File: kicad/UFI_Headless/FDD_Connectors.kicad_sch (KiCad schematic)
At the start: 11 parts, among them J6 FDD_34PIN, J7 AMIGA_FDD

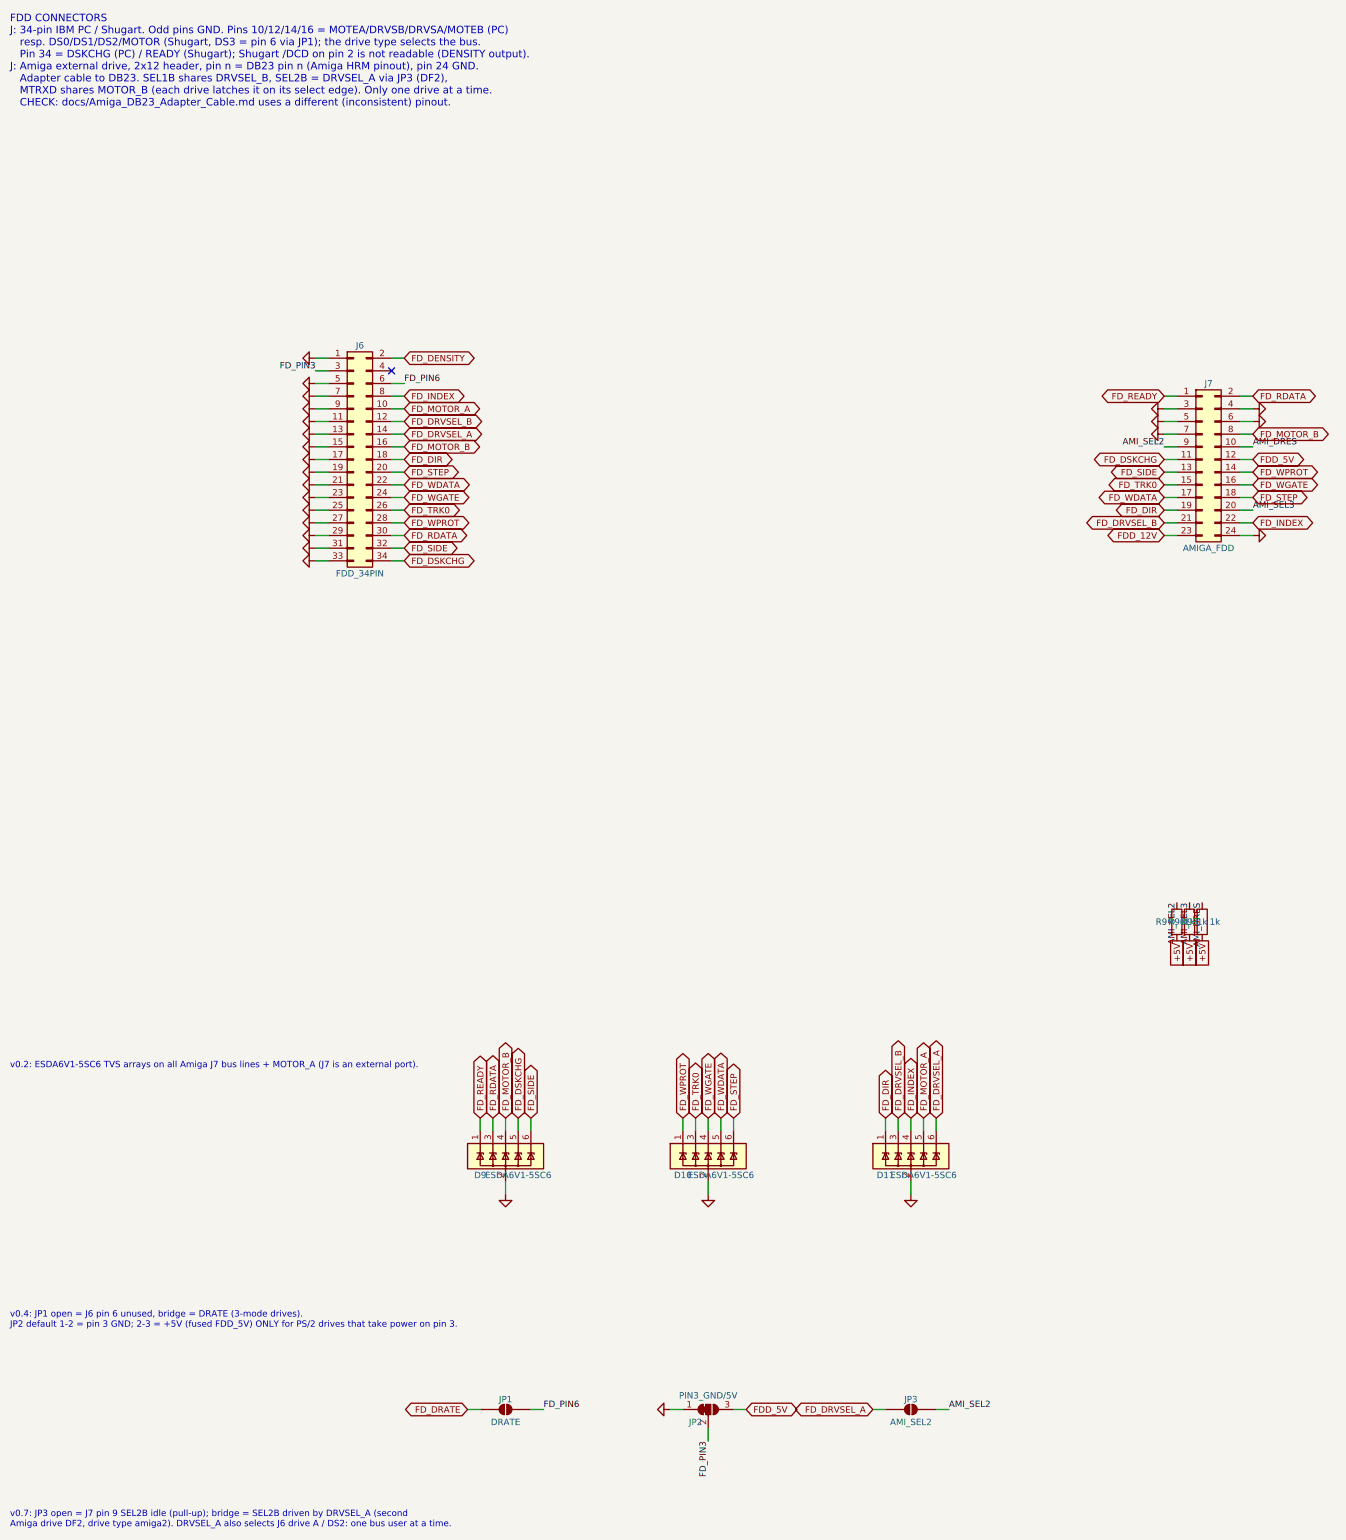
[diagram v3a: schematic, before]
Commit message: KiCad v0.7 rework, stage A11a (owner's device-comparison list M1, M4, M6): write lock gates both write requests, terminations on FDD_5V, JP2 gone - Flux_Interface: U14 becomes a 74LVC1G32 (Diodes 74LVC1G32SE-7 C460530, SOT-353; was the 74LVC1G332 of A9b) forming the global net LOCK = WLOCK_HW or WLOCK_FW; new U30 74LVC2G32 (Nexperia 74LVC2G32DP,125 C548635, TSSOP-8; single-unit project symbol UFI_Headless:74LVC2G32 because the KiCad multi-unit symbol does not work with the MCP placement, pinout 1 1A 2 1B 3 2Y 4 GND 5 2A 6 2B 7 1Y 8 VCC from the datasheet family) gates FDD_WGATE -> FDD_WGATE_G (U7 pin 3, TP8) and APL_WRREQ -> APL_WRREQ_G (new global net to U16 2A2 on Apple_Port, the MCU-side pull-up RN10 stays on APL_WRREQ), C84 100 nF; both requests are active low, LOCK high forces them inactive, so the Apple write request no longer bypasses the lock (netlist: LOCK = U14.4 U30.2 U30.6, APL_WRREQ_G = U16.13 U30.3, FDD_WGATE_G = U7.3 U30.7 TP8.1). M4: R75-R91 (Flux_Interface) and R97-R99 (FDD_Connectors, same reason) pull up to FDD_5V instead of +5V, R92-R96 on the IEC bus stay at +5V. M6: JP2 with its GND symbol and labels removed, J6 pin 3 is GND. Note on the sheet. ERC over the whole project 0 errors / 0 warnings (build/erc.rpt). No firmware change (WLOCK_FW/WLOCK_HW semantics unchanged). PLAN.md A11a done, kicad README A11a row. PCB follows in B3.
Claude-Session: https://claude.ai/code/session_014MdzrcyXuayppPHbfEjUrw
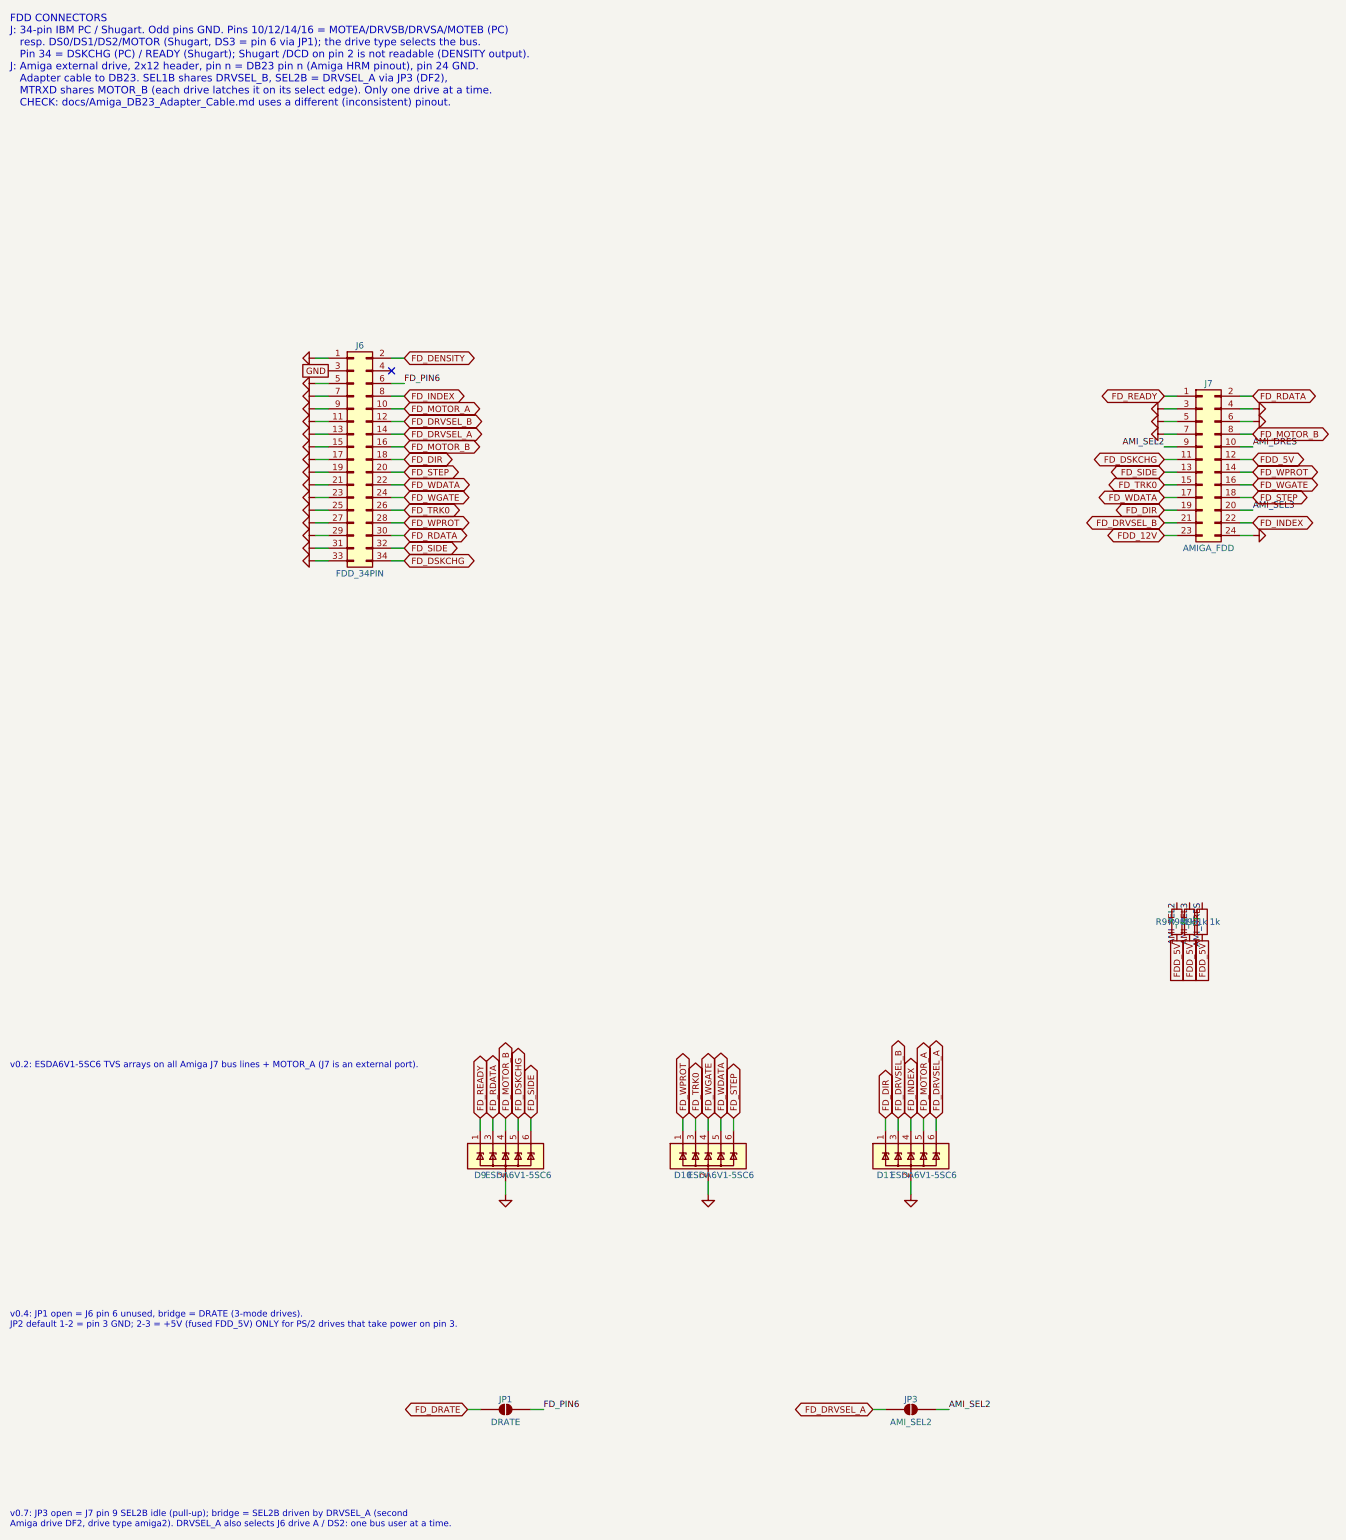
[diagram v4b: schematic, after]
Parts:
- removed JP2: PIN3_GND/5V, Jumper:SolderJumper-3_P1.3mm_Bridged12_RoundedPad1.0x1.5mm, symbol Jumper:SolderJumper_3_Bridged12
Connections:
- net +5V is gone; now on net FDD_5V: R97.2, R98.2, R99.2
- net FD_PIN3 is gone; now on net GND: J6.3 (Pin_3)
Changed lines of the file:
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@@
 		)
 	)
-	(wire
-		(pts
-			(xy 83.82 91.44) (xy 81.28 91.44)
-		)
-		(stroke
-			(width 0)
-			(type default)
-		)
-	)
-	(label "FD_PIN3"
-		(at 81.28 91.44 180)
-		(fields_autoplaced yes)
-		(effects
-			(font
-				(size 1.27 1.27)
-			)
-			(justify right bottom)
-		)
-	)
 	(no_connect
 		(at 96.52 91.44)
@@
 		)
 	)
-	(wire
-		(pts
-			(xy 154.94 299.72) (xy 152.4 299.72)
-		)
-		(stroke
-			(width 0)
-			(type default)
-		)
-	)
-	(wire
-		(pts
-			(xy 160.02 303.53) (xy 160.02 306.07)
-		)
-		(stroke
-			(width 0)
-			(type default)
-		)
-	)
-	(label "FD_PIN3"
-		(at 160.02 306.07 270)
-		(fields_autoplaced yes)
-		(effects
-			(font
-				(size 1.27 1.27)
-			)
-			(justify right bottom)
-		)
-	)
-	(wire
-		(pts
-			(xy 165.1 299.72) (xy 167.64 299.72)
-		)
-		(stroke
-			(width 0)
-			(type default)
-		)
-	)
-	(global_label "FDD_5V"
-		(shape bidirectional)
-		(at 167.64 299.72 0)
-		(fields_autoplaced yes)
-		(effects
-			(font
-				(size 1.27 1.27)
-			)
-			(justify left)
-		)
-		(property "Intersheetrefs" "${INTERSHEET_REFS}"
-			(at 167.64 299.72 0)
-			(effects
-				(font
-					(size 1.27 1.27)
-				)
-				(hide yes)
-			)
-		)
-	)
 	(text "v0.7: JP3 open = J7 pin 9 SEL2B idle (pull-up); bridge = SEL2B driven by DRVSEL_A (second\nAmiga drive DF2, drive type amiga2). DRVSEL_A also selects J6 drive A / DS2: one bus user at a time."
 		(exclude_from_sim no)
@@
 	)
 	(symbol
-		(lib_id "power:GND")
-		(at 152.4 299.72 270)
-		(unit 1)
-		(exclude_from_sim no)
-		(in_bom no)
-		(on_board yes)
-		(dnp no)
-		(property "Reference" "#PWR259"
-			(at 152.4 299.72 0)
-			(effects
-				(font
-					(size 1.27 1.27)
-				)
-				(hide yes)
-			)
-		)
-		(property "Value" "GND"
-			(at 152.4 299.72 0)
-			(effects
-				(font
-					(size 1.27 1.27)
-				)
-				(hide yes)
-			)
-		)
-		(property "Footprint" ""
-			(at 152.4 299.72 0)
-			(effects
-				(font
-					(size 1.27 1.27)
-				)
-				(hide yes)
-			)
-		)
-		(property "Datasheet" ""
-			(at 152.4 299.72 0)
-			(effects
-				(font
-					(size 1.27 1.27)
-				)
-				(hide yes)
-			)
-		)
-		(pin "1"
-		)
-		(instances
-			(project "UFI_Headless"
-				(path "/dc1b800d-cedf-5627-97f0-e6992ff33669/7efa7110-e20d-5bc0-a817-7dc9a25f889d"
-					(reference "#PWR259")
-					(unit 1)
-				)
-			)
-		)
-	)
-	(symbol
-		(lib_id "Jumper:SolderJumper_3_Bridged12")
-		(at 160.02 299.72 0)
-		(unit 1)
-		(exclude_from_sim no)
-		(in_bom no)
-		(on_board yes)
-		(dnp no)
-		(property "Reference" "JP2"
-			(at 157.48 302.26 0)
-			(effects
-				(font
-					(size 1.27 1.27)
-				)
-			)
-		)
-		(property "Value" "PIN3_GND/5V"
-			(at 160.02 296.926 0)
-			(effects
-				(font
-					(size 1.27 1.27)
-				)
-			)
-		)
-		(property "Footprint" "Jumper:SolderJumper-3_P1.3mm_Bridged12_RoundedPad1.0x1.5mm"
-			(at 160.02 299.72 0)
-			(effects
-				(font
-					(size 1.27 1.27)
-				)
-				(hide yes)
-			)
-		)
-		(property "Datasheet" ""
-			(at 160.02 314.96 0)
-			(effects
-				(font
-					(size 1.27 1.27)
-				)
-				(hide yes)
-			)
-		)
-		(pin "1"
-		)
-		(pin "2"
-		)
-		(pin "3"
-		)
-		(instances
-			(project "UFI_Headless"
-				(path "/dc1b800d-cedf-5627-97f0-e6992ff33669/7efa7110-e20d-5bc0-a817-7dc9a25f889d"
-					(reference "JP2")
-					(unit 1)
-				)
-			)
-		)
-	)
-	(symbol
 		(lib_id "Jumper:SolderJumper_2_Open")
 		(at 200.66 299.72 0)
@@
 		)
 	)
-	(global_label "+5V"
+	(global_label "FDD_5V"
 		(at 254.0 205.74 270)
 		(effects
@@
 		)
 	)
-	(global_label "+5V"
+	(global_label "FDD_5V"
 		(at 256.54 205.74 270)
 		(effects
@@
 		)
 	)
-	(global_label "+5V"
+	(global_label "FDD_5V"
 		(at 259.08 205.74 270)
 		(effects
 			(font
+				(size 1.27 1.27)
+			)
+			(justify right)
+		)
+	)
+	(global_label "GND"
+		(at 83.82000000000001 91.44 180)
+		(effects
+			(font

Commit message: KiCad v0.7 rework, stage A11d part 1 (owner's device-comparison list M5, S1-S4, S6; pins per docs/Timer_Zuteilung.md): sync sensor, J6 pin 2/4/33, rail voltage sense - Apple_Port: J19 pin 3 leaves the INDEX bus and becomes SYNC_5V with R165 10k to +3V3 and D30 PESD3V3L1BA, the new third Schmitt inverter U26 74LVC14AD (C133541, single-unit project symbol UFI_Headless:74LVC14_1U) turns it into SYNC -> PC6 (TIM8_CH1, AF3), also reads J6 pin 2 (FD_DENSITY) and pin 4 (FD_PIN4) back as FDD_PIN2_IN -> PD14 / FDD_PIN4_IN -> PD15 and reserves input 9 for the Mac !CSTOUT line of K1 (no-connect until A11d part 2), unused inputs on GND, C86 100 nF. FDD_Connectors: J6 pin 4 gets its own open-drain output Q12 BSS138DW (C154900, channel 1, gate FDD_PIN4 = PF14 with R158 100k, termination R159 1k to FDD_5V); J6 pin 33 moves from a fixed GND to the solder jumper JP7 (bridged to GND by default) whose third pad carries FLIPPY = PB5 through R156 2.2k with R157 2.2k to GND (2.2k instead of the planned 2.4k because 2.2k C4190 is already in the BOM). Power: R160/R161 10k/10k (FDD_5V / 2 -> V_FDD5 = PC4, ADC1 INP4) and R162/R163 33k/10k (FDD_12V / 4.3 -> V_FDD12 = PC5, ADC1 INP8). MCU_Core: no-connects on PC6, PD14, PD15, PF14, PB5, PC4, PC5, PB1 replaced by the global labels; PB0 (MAC_SEL) and PA8 (MAC_PWM) stay no-connect until the Mac header comes in part 2, PB1 = MAC_CSTOUT is already wired to U26. ERC over the whole project 0 errors / 0 warnings (build/erc.rpt). Firmware in the same commit: board.h/board_headless.c define PIN_SYNC, PIN_FDD_PIN2_IN, PIN_FDD_PIN4_IN, PIN_FDD_PIN4, PIN_FDD_PIN33, PIN_MAC_SEL, PIN_MAC_PWM, PIN_MAC_CSTOUT and ADC_CH_V_FDD5/V_FDD12 and initialise them as inputs or released (low) outputs; the TIM8 capture of SYNC, the rail-voltage limits (4.5 V / 10.8 V) and the protocol access follow in stage A10 (protocol doc: one hunk in the INDEX_SIM bullet - the sync sensor no longer drives the INDEX bus on v1.0, apple_sync has no effect there until A10). ARM build 0 wa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
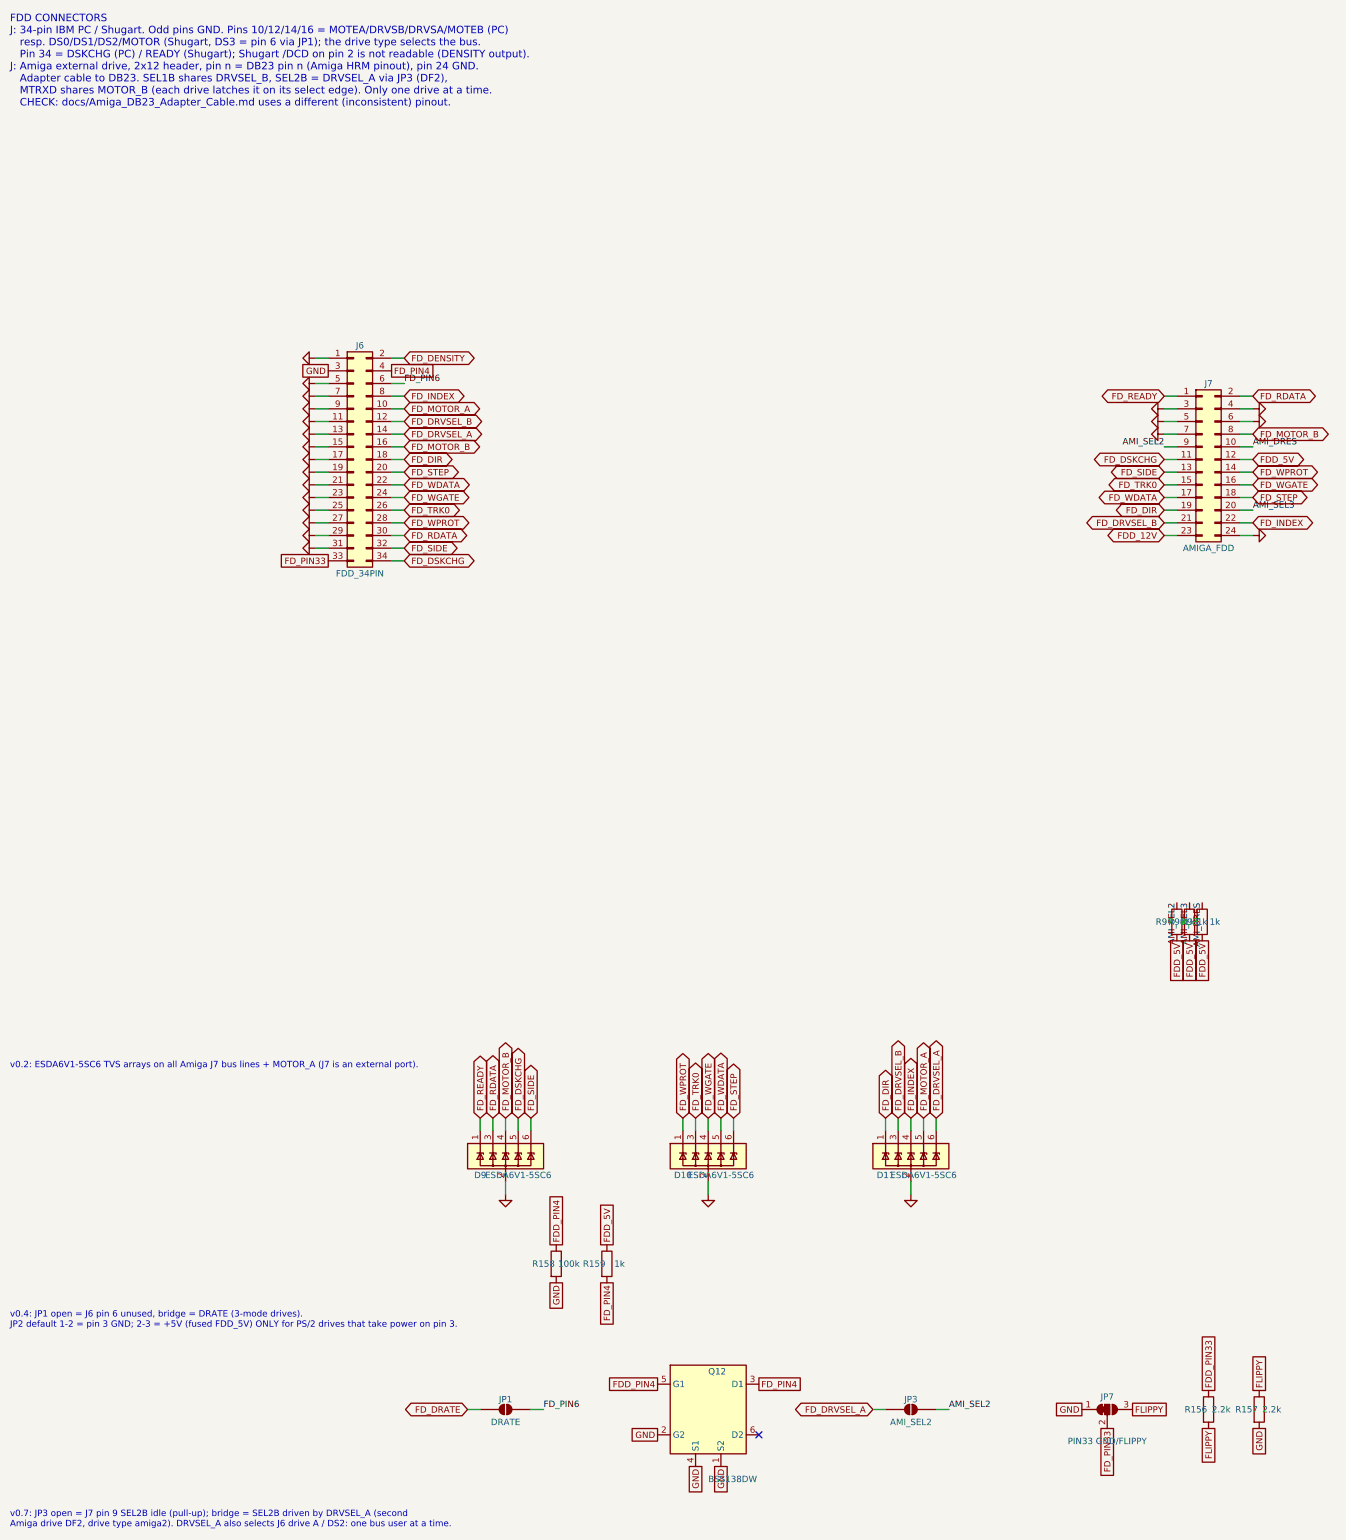
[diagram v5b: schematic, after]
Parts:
- added JP7: PIN33 GND/FLIPPY, Jumper:SolderJumper-3_P1.3mm_Bridged12_RoundedPad1.0x1.5mm, symbol Jumper:SolderJumper_3_Bridged12
- added Q12: BSS138DW, Package_TO_SOT_SMD:SOT-363_SC-70-6, symbol UFI_Headless:BSS138DW
- added R156, R157: 2.2k, Resistor_SMD:R_0603_1608Metric, symbol Device:R
- added R158: 100k, Resistor_SMD:R_0603_1608Metric, symbol Device:R
- added R159: 1k, Resistor_SMD:R_0603_1608Metric, symbol Device:R
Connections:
- net FDD_5V: now also R159.1
- net GND: now also JP7.1 (A), Q12.1 (S2), Q12.2 (G2), Q12.4 (S1), R157.2, R158.2; no longer J6.33 (Pin_33)
- net FD_PIN4: now reaches J6.4 (Pin_4)
- net FD_PIN4: now also Q12.3 (D1), R159.2
- new net FDD_PIN33: R156.1
- new net FDD_PIN4: Q12.5 (G1), R158.1
- new net FD_PIN33: J6.33 (Pin_33), JP7.2 (C)
- new net FLIPPY: JP7.3 (B), R156.2, R157.1
